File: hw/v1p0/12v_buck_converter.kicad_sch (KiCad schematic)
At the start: 19 parts, among them J9 Test Points, U8 TPS54331DR

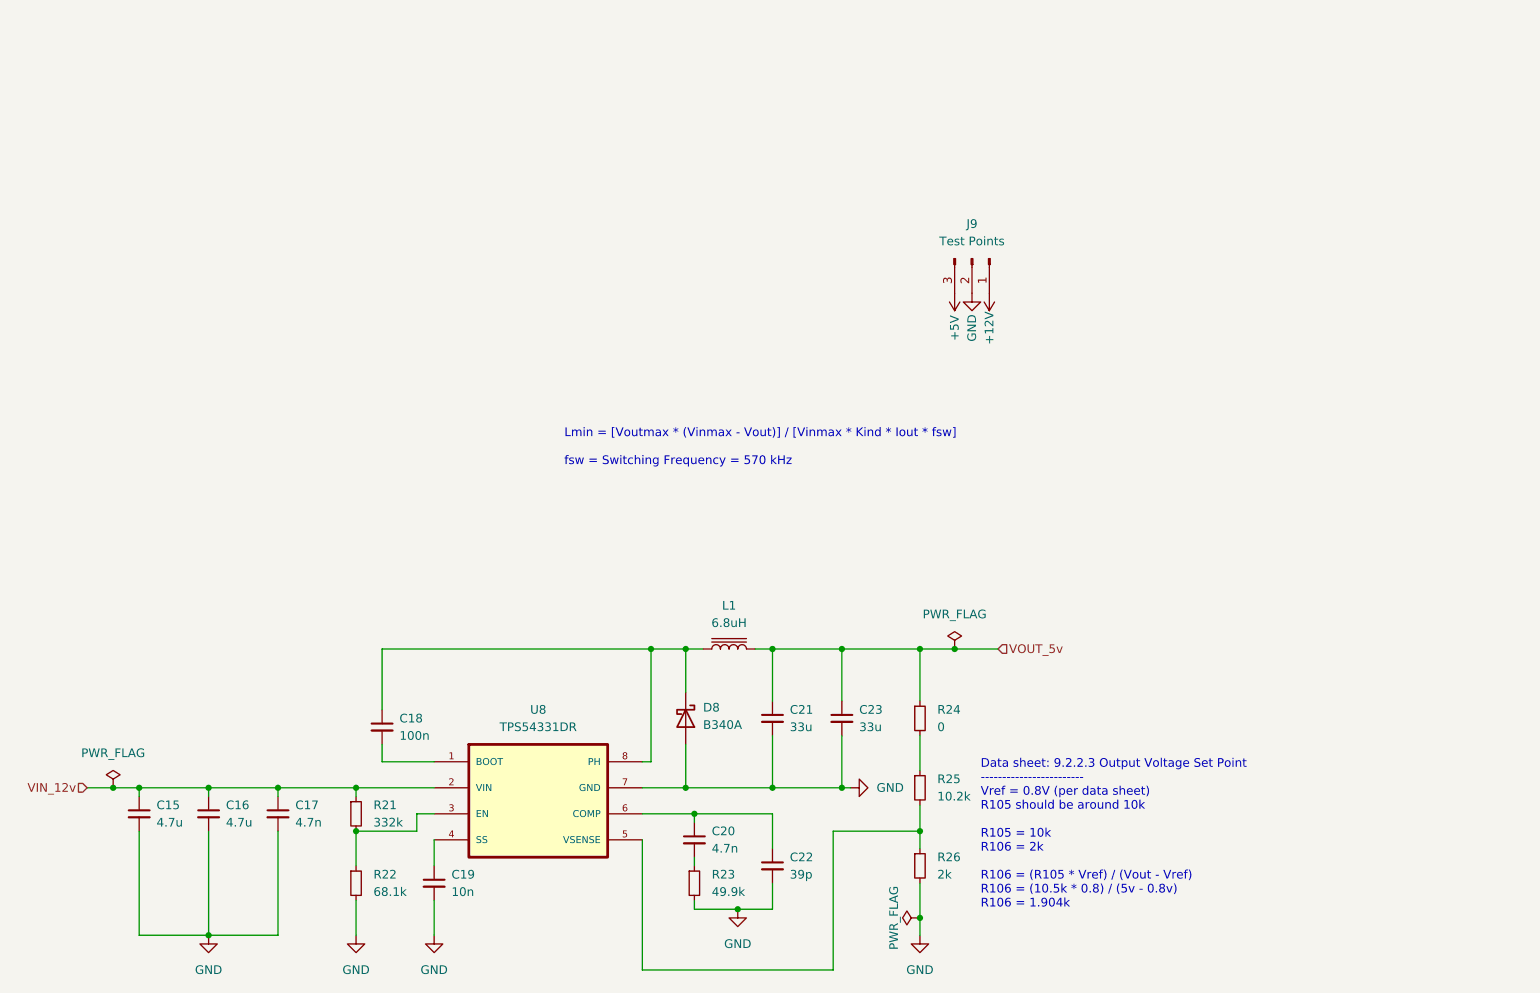
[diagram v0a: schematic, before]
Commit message: Last version before removing mosfet
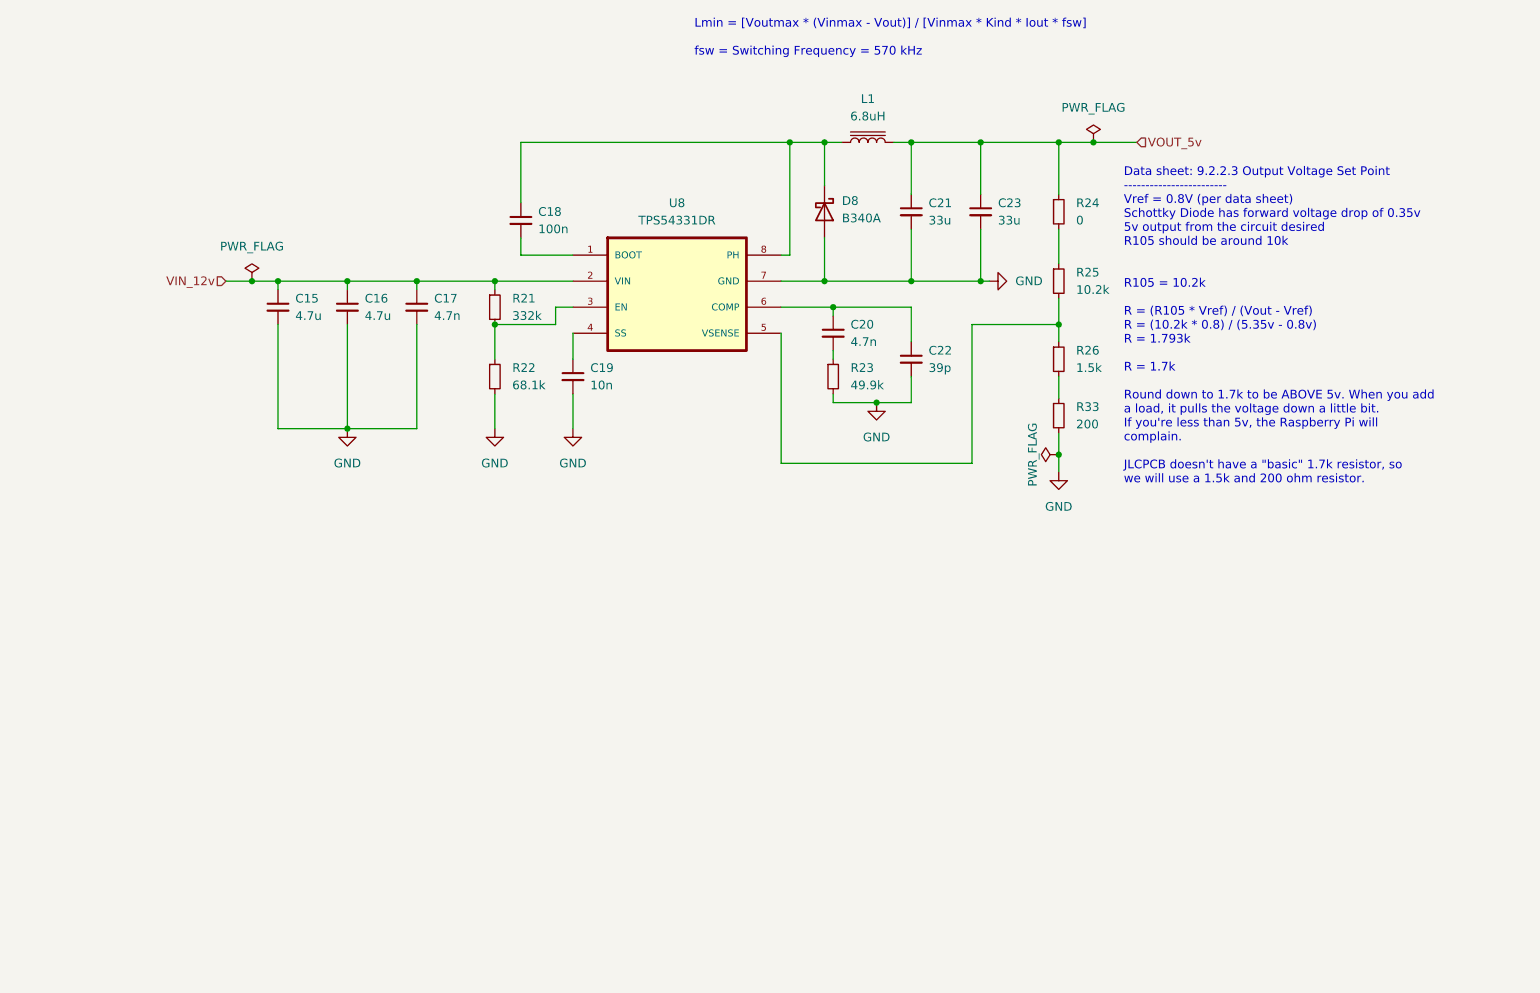
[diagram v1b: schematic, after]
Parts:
- removed J9: Test Points, Connector_PinHeader_2.54mm:PinHeader_1x03_P2.54mm_Vertical, symbol Connector:Conn_01x03_Male
- added R33: 200, Resistor_SMD:R_0805_2012Metric, symbol Device:R_Small
- R26: value 2k -> 1.5k; LCSC C17604 -> C4310
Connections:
- net GND: now also R33.2; no longer R26.2
- new net: R26.2, R33.1
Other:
- note added: "Data sheet: 9.2.2.3 Output Voltage Set Point ------------------------ Vref = 0.8V (per data sheet) Schottky Diode has forward voltage drop of 0.35v 5v output from the circuit desired R105 should be around 10k R105 = 10.2k R = (R105 * Vref) / (Vout - Vref) R = (10.2k * 0.8) / (5.35v - 0.8v) R = 1.793k R = 1.7k Round down to 1.7k to be ABOVE 5v. When you add a load, it pulls the voltage down a litt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"
- note removed: "Data sheet: 9.2.2.3 Output Voltage Set Point ------------------------ Vref = 0.8V (per data sheet) R105 should be around 10k R105 = 10k R106 = 2k R106 = (R105 * Vref) / (Vout - Vref) R106 = (10.5k * 0.8) / (5v - 0.8v) R106 = 1.904k"
- moved on the sheet: C15, C16, C17, C18, C19, C20, C21, C22, C23, D8, L1, R21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

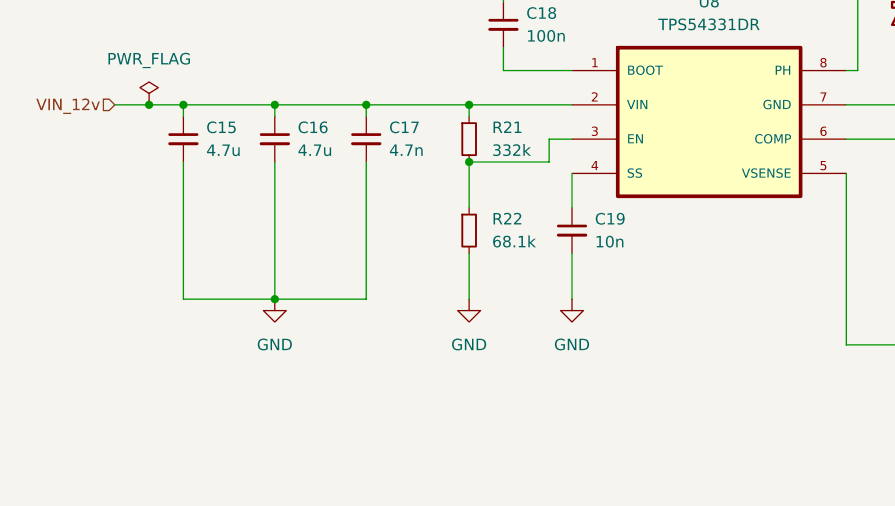
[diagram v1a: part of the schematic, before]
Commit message: Removed Mosfet - release candidate 1.0
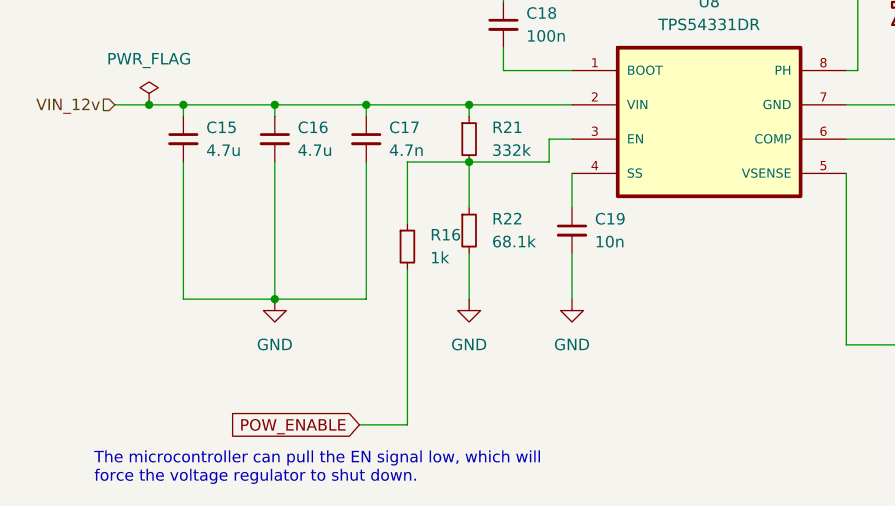
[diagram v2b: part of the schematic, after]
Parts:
- added R16: 1k, Resistor_SMD:R_0805_2012Metric, symbol Device:R_Small
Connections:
- net at R21.2, R22.1, U8.3 (EN): now also R16.1
- new net POW_ENABLE: R16.2
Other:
- note added: "The microcontroller can pull the EN signal low, which will force the voltage regulator to shut down."
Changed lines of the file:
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@@
     (stroke (width 0) (type default) (color 0 0 0 0))
   )
-  (wire (pts (xy 102.87 68.072) (xy 93.98 68.072))
+  (wire (pts (xy 93.98 68.072) (xy 102.87 68.072))
     (stroke (width 0) (type default) (color 0 0 0 0))
   )
@@
     (stroke (width 0) (type default) (color 0 0 0 0))
   )
+  (wire (pts (xy 87.122 97.282) (xy 81.788 97.282))
+    (stroke (width 0) (type default) (color 0 0 0 0))
+  )
   (wire (pts (xy 163.83 68.072) (xy 176.53 68.072))
     (stroke (width 0) (type default) (color 0 0 0 0))
@@
     (stroke (width 0) (type default) (color 0 0 0 0))
   )
+  (wire (pts (xy 87.122 80.01) (xy 87.122 97.282))
+    (stroke (width 0) (type default) (color 0 0 0 0))
+  )
   (wire (pts (xy 93.98 68.072) (xy 93.98 73.152))
     (stroke (width 0) (type default) (color 0 0 0 0))
@@
     (stroke (width 0) (type default) (color 0 0 0 0))
   )
+  (wire (pts (xy 87.122 68.072) (xy 93.98 68.072))
+    (stroke (width 0) (type default) (color 0 0 0 0))
+  )
   (wire (pts (xy 82.55 83.312) (xy 72.39 83.312))
     (stroke (width 0) (type default) (color 0 0 0 0))
@@
     (stroke (width 0) (type default) (color 0 0 0 0))
   )
+  (wire (pts (xy 87.122 74.93) (xy 87.122 68.072))
+    (stroke (width 0) (type default) (color 0 0 0 0))
+  )
   (wire (pts (xy 154.94 79.502) (xy 154.94 75.692))
     (stroke (width 0) (type default) (color 0 0 0 0))
@@
   (wire (pts (xy 93.98 61.722) (xy 105.41 61.722))
     (stroke (width 0) (type default) (color 0 0 0 0))
+  )
+  (text "The microcontroller can pull the EN signal low, which will\nforce the voltage regulator to shut down."
+    (at 52.324 103.886 0)
+    (effects (font (size 1.27 1.27)) (justify left bottom))
   )
   (text "Data sheet: 9.2.2.3 Output Voltage Set Point\n------------------------\nVref = 0.8V (per data sheet)\nSchottky Diode has forward voltage drop of 0.35v\n5v output from the circuit desired\nR105 should be around 10k\n\n\nR105 = 10.2k\n\nR = (R105 * Vref) / (Vout - Vref)\nR = (10.2k * 0.8) / (5.35v - 0.8v)\nR = 1.793k\n\nR = 1.7k\n\nRound down to 1.7k to be ABOVE 5v. When you add \na load, it pulls the voltage down a little bit. \nIf you're less than 5v, the Raspberry Pi will \ncomplain.\n\nJLCPCB doesn't have a \"basic\" 1.7k resistor, so \nwe will use a 1.5k and 200 ohm resistor."
@@
     (effects (font (size 1.27 1.27)) (justify left bottom))
   )
+  (global_label "POW_ENABLE" (shape input) (at 81.788 97.282 180) (fields_autoplaced)
+    (effects (font (size 1.27 1.27)) (justify right))
+    (property "Intersheet References" "${INTERSHEET_REFS}" (id 0) (at 67.3401 97.3614 0)
+      (effects (font (size 1.27 1.27)) (justify right) hide)
+    )
+  )
   (hierarchical_label "VIN_12v" (shape input) (at 54.61 61.722 180)
     (effects (font (size 1.27 1.27)) (justify right))
@@
       (effects (font (size 1.27 1.27)) hide)
     )
+    (pin "1")
+    (pin "2")
+  )
+  (symbol (lib_id "Device:R_Small") (at 87.122 77.47 0) (unit 1)
+    (in_bom yes) (on_board yes) (fields_autoplaced)
+    (property "Reference" "R16" (id 0) (at 89.662 76.1999 0)
+      (effects (font (size 1.27 1.27)) (justify left))
+    )
+    (property "Value" "1k" (id 1) (at 89.662 78.7399 0)
+      (effects (font (size 1.27 1.27)) (justify left))
+    )
+    (property "Footprint" "Resistor_SMD:R_0805_2012Metric" (id 2) (at 87.122 77.47 0)
+      (effects (font (size 1.27 1.27)) hide)
+    )
+    (property "Datasheet" "~" (id 3) (at 87.122 77.47 0)
+      (effects (font (size 1.27 1.27)) hide)
+    )
+    (property "DigikeyPN" "CF14JT1K00CT-ND" (id 4) (at 87.122 77.47 0)
+      (effects (font (size 1.27 1.27)) hide)
+    )
+    (property "LCSC" "C17513" (id 5) (at 87.122 77.47 0)
+      (effects (font (size 1.27 1.27)) hide)
+    )

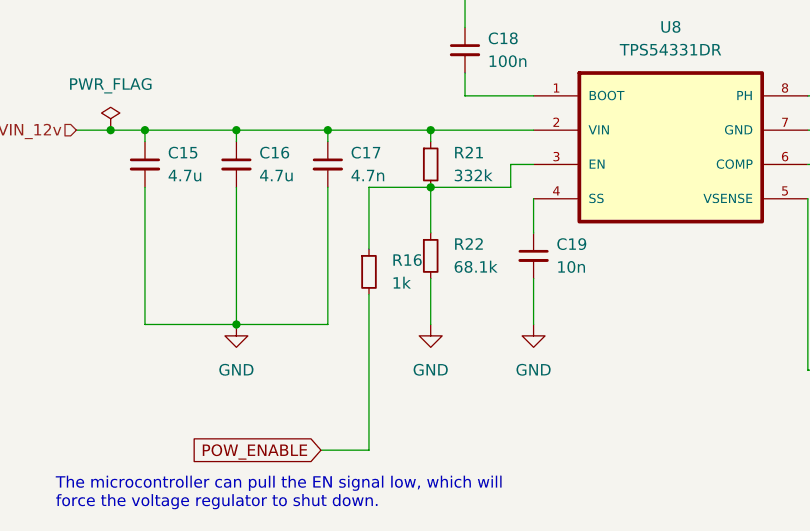
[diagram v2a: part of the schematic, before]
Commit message: Change power control resistor to jumper
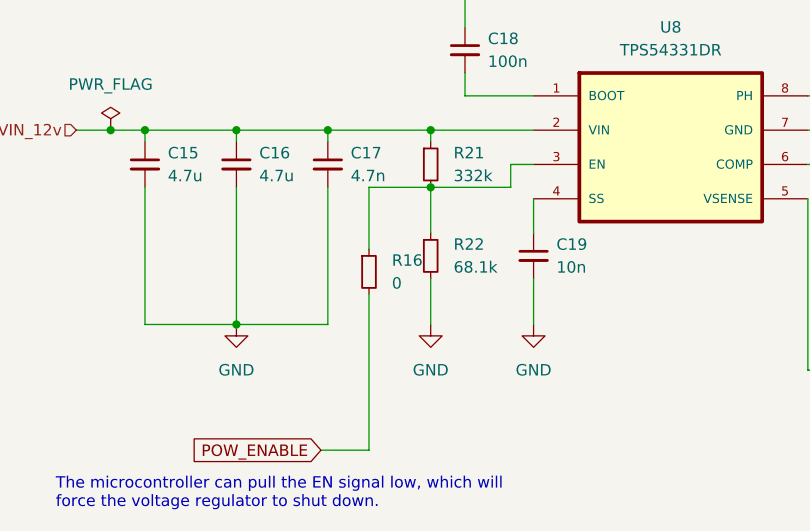
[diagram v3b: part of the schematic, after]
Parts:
- R16: value 1k -> 0; LCSC C17513 -> C17477
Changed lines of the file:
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@@
       (effects (font (size 1.27 1.27)) (justify left))
     )
-    (property "Value" "1k" (id 1) (at 89.662 78.7399 0)
+    (property "Value" "0" (id 1) (at 89.662 78.7399 0)
       (effects (font (size 1.27 1.27)) (justify left))
     )
@@
       (effects (font (size 1.27 1.27)) hide)
     )
-    (property "LCSC" "C17513" (id 5) (at 87.122 77.47 0)
+    (property "LCSC" "C17477" (id 5) (at 87.122 77.47 0)
       (effects (font (size 1.27 1.27)) hide)
     )

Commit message: As-Ordered version
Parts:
- C21, C23: LCSC C342635 -> C432920
- D8: value B340A -> SS54; LCSC C64982 -> C22452
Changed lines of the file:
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@@
       (effects (font (size 1.27 1.27)) hide)
     )
-    (property "LCSC" "C342635" (id 4) (at 154.94 51.562 0)
+    (property "LCSC" "C432920" (id 4) (at 154.94 51.562 0)
       (effects (font (size 1.27 1.27)) hide)
     )
@@
       (effects (font (size 1.27 1.27)) (justify left))
     )
-    (property "Value" "B340A" (id 1) (at 144.78 52.5144 90)
+    (property "Value" "SS54" (id 1) (at 144.78 52.5144 90)
       (effects (font (size 1.27 1.27)) (justify left))
     )
@@
       (effects (font (size 1.27 1.27)) hide)
     )
-    (property "Datasheet" "http://www.jameco.com/Jameco/Products/ProdDS/1538777.pdf" (id 3) (at 142.24 51.562 0)
+    (property "Datasheet" "https://datasheet.lcsc.com/lcsc/1810192041_MDD-Microdiode-Electronics--SS54_C22452.pdf" (id 3) (at 142.24 51.562 0)
       (effects (font (size 1.27 1.27)) hide)
     )
-    (property "LCSC" "C64982" (id 4) (at 142.24 51.562 90)
+    (property "LCSC" "C22452" (id 4) (at 142.24 51.562 90)
       (effects (font (size 1.27 1.27)) hide)
     )
@@
       (effects (font (size 1.27 1.27)) hide)
     )
-    (property "LCSC" "C342635" (id 4) (at 165.1 51.562 0)
+    (property "LCSC" "C432920" (id 4) (at 165.1 51.562 0)
       (effects (font (size 1.27 1.27)) hide)
     )
